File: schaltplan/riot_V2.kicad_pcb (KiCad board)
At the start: 2 copper layers, 29 x 30.3 mm, 17 parts, among them J1 valve_connector_1, J2 battery_connector, J3 valve_connector_2, J4 Conn_01x10_Male_I2C_SPI_plus, Q1 AO3400A, Q2 AO3400A, U1 bme280_board, U2 dcdc_any_to_3v3, U3 dcdc_any_to_5v, U4 ESP32-WROOM-32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

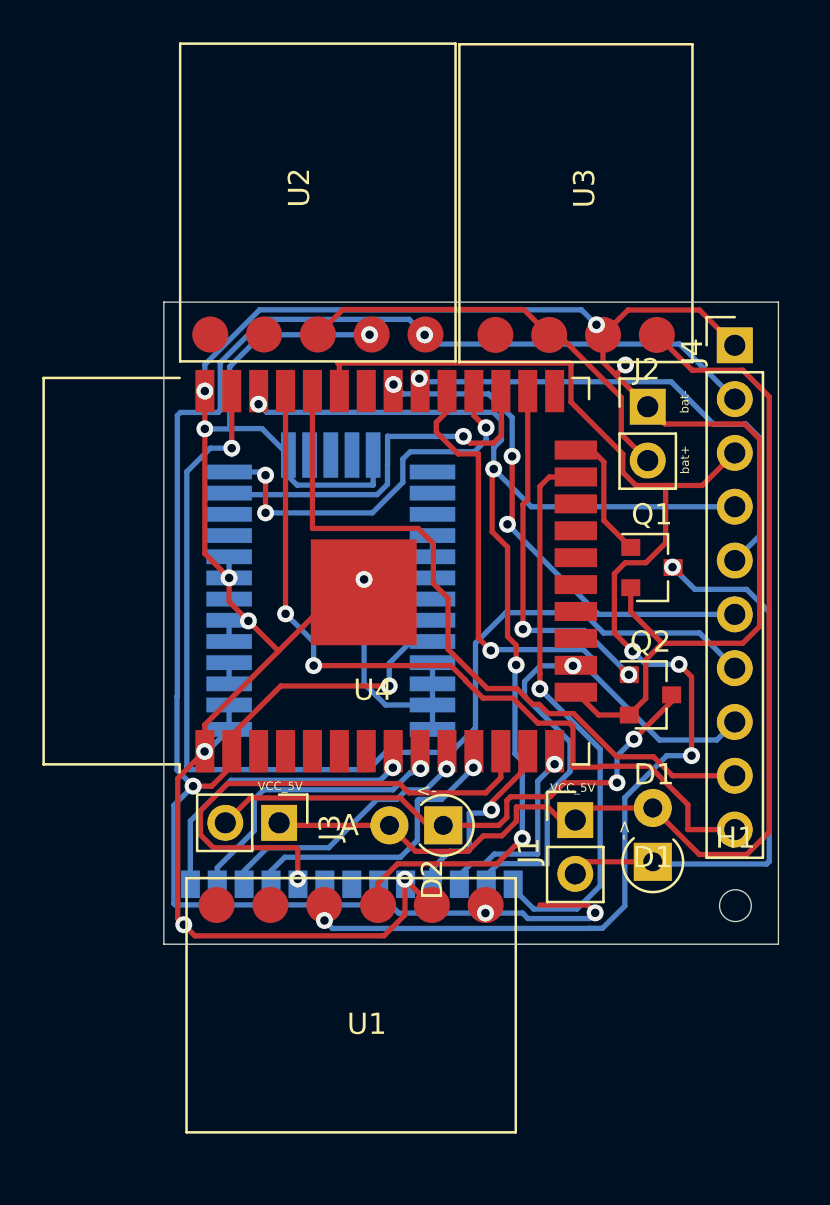
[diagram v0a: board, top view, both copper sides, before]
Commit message: Add en and io0 pin to mini-loon board
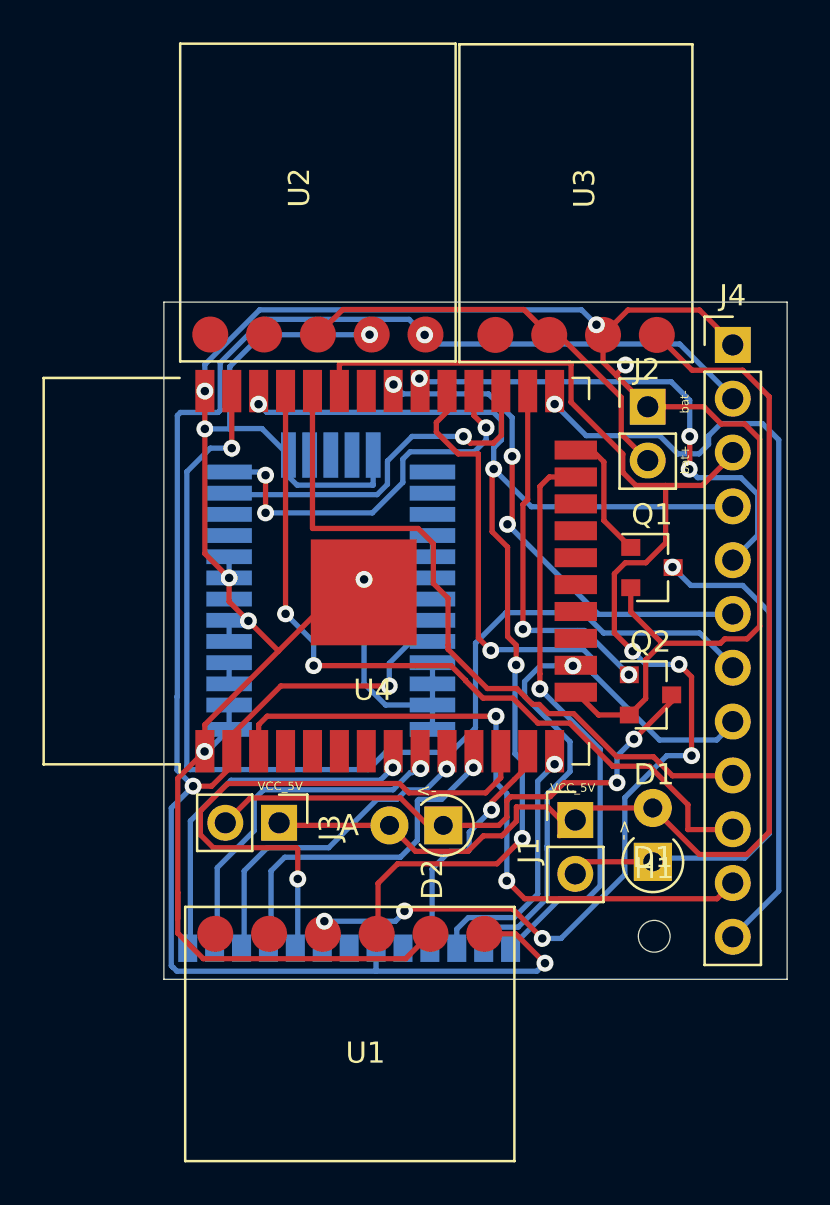
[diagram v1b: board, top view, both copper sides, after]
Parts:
- J4: value Conn_01x10_Male_I2C_SPI_plus -> Conn_01x12_Male; footprint Connector_PinHeader_2.54mm:PinHeader_1x10_P2.54mm_Vertical -> Connector_PinHeader_2.54mm:PinHeader_1x12_P2.54mm_Vertical
- moved H1 4.10 mm to (108.4, 108.6)
- moved U6 3.02 mm to (94.1, 117.0)
- moved U1 1.36 mm to (93.8, 113.0)
- moved J4 0.10 mm to (112.1, 80.7)
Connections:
- U4 pad 25: Net-(U4-Pad25) -> ESP_IO0
- U4 pad 3: Net-(U4-Pad3) -> ESP_EN
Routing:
- net ESP_IO0: track 0.00 -> 37.1 mm, vias 0 -> 1
- net ESP_EN: track 0.00 -> 31.9 mm, vias 0 -> 2
- net ESP_GPIO27: track 23.9 -> 27.2 mm
- net ESP_HSPI_MISO: track 9.87 -> 12.8 mm
- net ESP_GPIO26: track 13.6 -> 16.4 mm
- net ESP_GPIO25: track 12.5 -> 15.3 mm
- net ESP_GPIO33: track 13.5 -> 16.3 mm
- net ESP_GPIO32: track 13.9 -> 16.7 mm
- net ESP_HSPI_MOSI: track 16.3 -> 19.0 mm
- net ESP_HSPI_SCK: track 9.36 -> 11.9 mm
- net ESP_I2C_SCL: track 53.5 -> 54.6 mm
- net ESP_U0TXD: track 38.5 -> 37.3 mm
- net VCC_3V3: track 94.8 -> 95.8 mm, vias 5 -> 4
- net /Valve_1_DRAIN: track 26.7 -> 26.0 mm
- net ESP_U2RXD: track 17.9 -> 17.2 mm
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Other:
- board size 29 x 30.3 mm -> 29.4 x 32 mm
